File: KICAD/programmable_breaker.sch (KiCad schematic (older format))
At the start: 43 parts, among them Q1 BC847, Q2 BC847, Q3 BC847, U2 LM2903

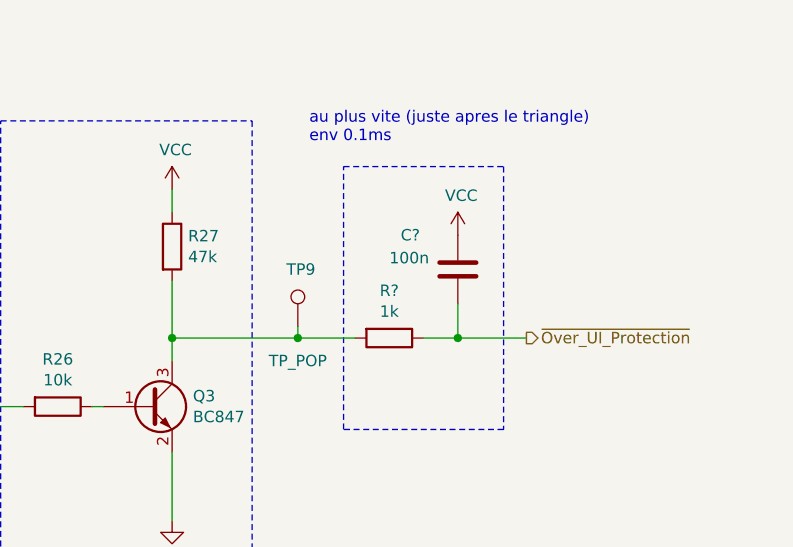
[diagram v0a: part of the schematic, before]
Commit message: edit footprints by jmt
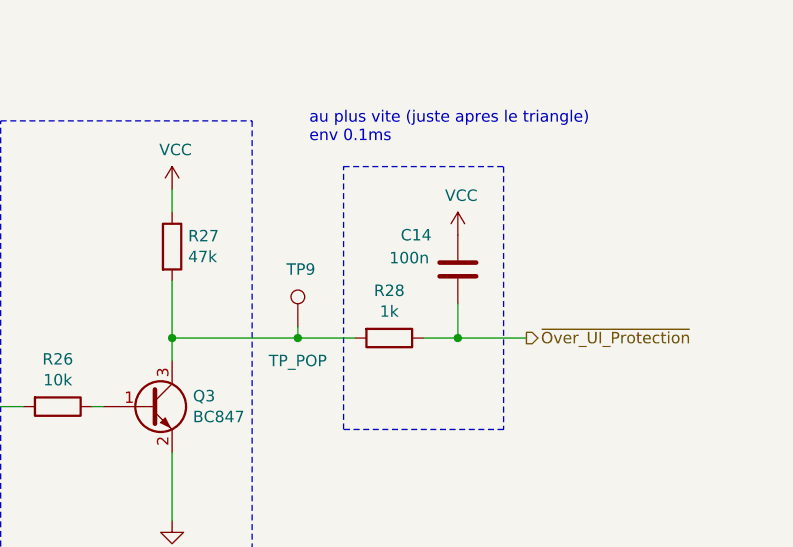
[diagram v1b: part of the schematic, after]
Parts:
- C10, C11, C6, C7, C8, C9: footprint (none) -> Capacitor_SMD:C_0805_2012Metric_Pad1.15x1.40mm_HandSolder
- C14: renamed from C?; footprint (none) -> Capacitor_SMD:C_0805_2012Metric_Pad1.15x1.40mm_HandSolder
- JP4, JP5, JP6, JP7, JP8, JP9: footprint (none) -> Connector_PinHeader_2.54mm:PinHeader_1x02_P2.54mm_Vertical
- R10, R11, R12, R13, R14, R15, R16, R17, R18, R19, R20, R21, R22, R23, R24, R25, R26, R27: footprint (none) -> Resistor_SMD:R_0805_2012Metric_Pad1.15x1.40mm_HandSolder
- R28: renamed from R?; footprint (none) -> Resistor_SMD:R_0805_2012Metric_Pad1.15x1.40mm_HandSolder
- TP5, TP6, TP8: footprint (none) -> TestPoint:TestPoint_THTPad_D2.0mm_Drill1.0mm
- TP7, TP9: footprint (none) -> TestPoint:TestPoint_Loop_D1.80mm_Drill1.0mm_Beaded
- U2: footprint (none) -> Package_SO:SO-8_5.3x6.2mm_P1.27mm

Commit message: route + work on djd
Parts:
- removed R28: 1k, Resistor_SMD:R_0805_2012Metric_Pad1.15x1.40mm_HandSolder, symbol Device:R
- C14: value 100n -> 470n
- R27: value 47k -> 10k
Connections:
- net GND: now also R27.2; no longer Q3.2 (E)
- net Rearm: now also Q1.1 (B), R24.1; no longer Q2.1 (B), R23.2
- net VCC: now also Q3.3 (C); no longer R27.1
- net ~Over_UI_Protection: now also Q3.2 (E), R27.1, TP9.1
- net at Q1.3 (C), R22.2, R23.1: no longer C11.1
- net S: now reaches TP7.1, U2.1, U2.7
- net S: now also Q2.1 (B), R23.2; no longer Q1.1 (B), R24.1
- net at Q2.3 (C), R24.2, R25.2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: now also C11.1
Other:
- note added: "4.7ms"
- note added: "47ms"
- note added: "A VOIR"
- note added: "Signal amp. & soft start"
- note removed: "Signal amp. & Invert"
- note removed: "au plus vite (juste apres le triangle)\nenv 0.1ms"
- moved on the sheet: C11, C14, Q1, Q2, Q3, R22, R23, R24, R25, R26, TP8, TP9

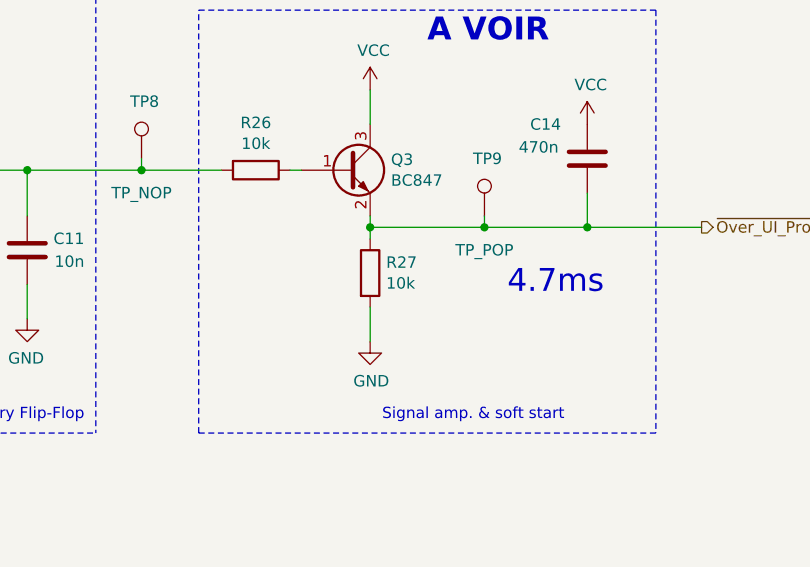
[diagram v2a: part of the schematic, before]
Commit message: added footprint for sepic coil + no more errors in netlist
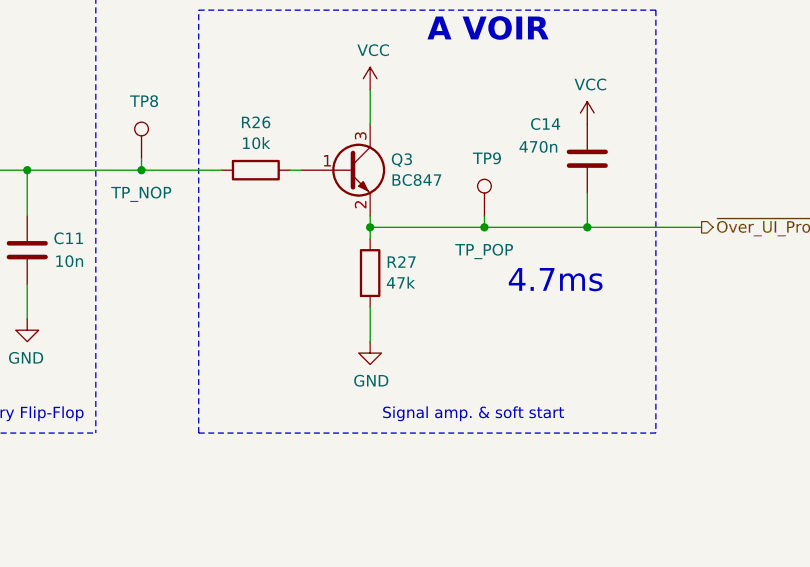
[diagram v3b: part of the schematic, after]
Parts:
- C10, C11, C14, C6, C7, C8, C9: footprint Capacitor_SMD:C_0805_2012Metric_Pad1.15x1.40mm_HandSolder -> Sesame_footprint:C_0805_2012Metric_Pad1.18x1.45mm_HandSolder
- R10, R11, R12, R13, R14, R15, R16, R17, R18, R19, R20, R21, R22, R23, R24, R25, R26: footprint Resistor_SMD:R_0805_2012Metric_Pad1.15x1.40mm_HandSolder -> Sesame_footprint:R_0805_2012Metric_Pad1.20x1.40mm_HandSolder
- R27: value 10k -> 47k; footprint Resistor_SMD:R_0805_2012Metric_Pad1.15x1.40mm_HandSolder -> Sesame_footprint:R_0805_2012Metric_Pad1.20x1.40mm_HandSolder
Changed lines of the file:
@@
 F 0 "R23" V 5957 2250 50  0000 C CNN
 F 1 "47k" V 5866 2250 50  0000 C CNN
-F 2 "Resistor_SMD:R_0805_2012Metric_Pad1.15x1.40mm_HandSolder" V 5680 2250 50  0001 C CNN
+F 2 "Sesame_footprint:R_0805_2012Metric_Pad1.20x1.40mm_HandSolder" V 5680 2250 50  0001 C CNN
 F 3 "~" H 5750 2250 50  0001 C CNN
 	1    5750 2250
@@
 F 0 "R24" V 6807 2250 50  0000 C CNN
 F 1 "47k" V 6716 2250 50  0000 C CNN
-F 2 "Resistor_SMD:R_0805_2012Metric_Pad1.15x1.40mm_HandSolder" V 6530 2250 50  0001 C CNN
+F 2 "Sesame_footprint:R_0805_2012Metric_Pad1.20x1.40mm_HandSolder" V 6530 2250 50  0001 C CNN
 F 3 "~" H 6600 2250 50  0001 C CNN
 	1    6600 2250
@@
 F 0 "R25" H 6970 1596 50  0000 L CNN
 F 1 "47k" H 6970 1505 50  0000 L CNN
-F 2 "Resistor_SMD:R_0805_2012Metric_Pad1.15x1.40mm_HandSolder" V 6830 1550 50  0001 C CNN
+F 2 "Sesame_footprint:R_0805_2012Metric_Pad1.20x1.40mm_HandSolder" V 6830 1550 50  0001 C CNN
 F 3 "~" H 6900 1550 50  0001 C CNN
 	1    6900 1550
@@
 F 0 "R22" H 5520 1596 50  0000 L CNN
 F 1 "47k" H 5520 1505 50  0000 L CNN
-F 2 "Resistor_SMD:R_0805_2012Metric_Pad1.15x1.40mm_HandSolder" V 5380 1550 50  0001 C CNN
+F 2 "Sesame_footprint:R_0805_2012Metric_Pad1.20x1.40mm_HandSolder" V 5380 1550 50  0001 C CNN
 F 3 "~" H 5450 1550 50  0001 C CNN
 	1    5450 1550
@@
 F 0 "C6" H 2765 6996 50  0000 L CNN
 F 1 "100n" H 2765 6905 50  0000 L CNN
-F 2 "Capacitor_SMD:C_0805_2012Metric_Pad1.15x1.40mm_HandSolder" H 2688 6800 50  0001 C CNN
+F 2 "Sesame_footprint:C_0805_2012Metric_Pad1.18x1.45mm_HandSolder" H 2688 6800 50  0001 C CNN
 F 3 "~" H 2650 6950 50  0001 C CNN
 	1    2650 6950
@@
 F 0 "R26" V 8143 2250 50  0000 C CNN
 F 1 "10k" V 8234 2250 50  0000 C CNN
-F 2 "Resistor_SMD:R_0805_2012Metric_Pad1.15x1.40mm_HandSolder" V 8280 2250 50  0001 C CNN
+F 2 "Sesame_footprint:R_0805_2012Metric_Pad1.20x1.40mm_HandSolder" V 8280 2250 50  0001 C CNN
 F 3 "~" H 8350 2250 50  0001 C CNN
 	1    8350 2250
@@
 F 0 "R20" V 3150 1850 50  0000 C CNN
 F 1 "100k" V 3050 1850 50  0000 C CNN
-F 2 "Resistor_SMD:R_0805_2012Metric_Pad1.15x1.40mm_HandSolder" V 2880 1850 50  0001 C CNN
+F 2 "Sesame_footprint:R_0805_2012Metric_Pad1.20x1.40mm_HandSolder" V 2880 1850 50  0001 C CNN
 F 3 "~" H 2950 1850 50  0001 C CNN
 	1    2950 1850
@@
 F 0 "C8" H 3515 2146 50  0000 L CNN
 F 1 "10n" H 3515 2055 50  0000 L CNN
-F 2 "Capacitor_SMD:C_0805_2012Metric_Pad1.15x1.40mm_HandSolder" H 3438 1950 50  0001 C CNN
+F 2 "Sesame_footprint:C_0805_2012Metric_Pad1.18x1.45mm_HandSolder" H 3438 1950 50  0001 C CNN
 F 3 "~" H 3400 2100 50  0001 C CNN
 	1    3400 2100
@@
 F 0 "R10" H 1020 2396 50  0000 L CNN
 F 1 "R" H 1020 2305 50  0000 L CNN
-F 2 "Resistor_SMD:R_0805_2012Metric_Pad1.15x1.40mm_HandSolder" V 880 2350 50  0001 C CNN
+F 2 "Sesame_footprint:R_0805_2012Metric_Pad1.20x1.40mm_HandSolder" V 880 2350 50  0001 C CNN
 F 3 "~" H 950 2350 50  0001 C CNN
 	1    950  2350
@@
 F 0 "R11" H 1020 2796 50  0000 L CNN
 F 1 "R" H 1020 2705 50  0000 L CNN
-F 2 "Resistor_SMD:R_0805_2012Metric_Pad1.15x1.40mm_HandSolder" V 880 2750 50  0001 C CNN
+F 2 "Sesame_footprint:R_0805_2012Metric_Pad1.20x1.40mm_HandSolder" V 880 2750 50  0001 C CNN
 F 3 "~" H 950 2750 50  0001 C CNN
 	1    950  2750
@@
 F 0 "R16" V 2300 1800 50  0000 C CNN
 F 1 "100k" V 2300 1600 50  0000 C CNN
-F 2 "Resistor_SMD:R_0805_2012Metric_Pad1.15x1.40mm_HandSolder" V 2330 1650 50  0001 C CNN
+F 2 "Sesame_footprint:R_0805_2012Metric_Pad1.20x1.40mm_HandSolder" V 2330 1650 50  0001 C CNN
 F 3 "~" H 2400 1650 50  0001 C CNN
 	1    2400 1650
@@
 F 0 "C7" H 3515 946 50  0000 L CNN
 F 1 "470n" H 3515 855 50  0000 L CNN
-F 2 "Capacitor_SMD:C_0805_2012Metric_Pad1.15x1.40mm_HandSolder" H 3438 750 50  0001 C CNN
+F 2 "Sesame_footprint:C_0805_2012Metric_Pad1.18x1.45mm_HandSolder" H 3438 750 50  0001 C CNN
 F 3 "~" H 3400 900 50  0001 C CNN
 	1    3400 900
@@
 F 0 "R14" V 2300 1300 50  0000 C CNN
 F 1 "100k" V 2300 1100 50  0000 C CNN
-F 2 "Resistor_SMD:R_0805_2012Metric_Pad1.15x1.40mm_HandSolder" V 2330 1150 50  0001 C CNN
+F 2 "Sesame_footprint:R_0805_2012Metric_Pad1.20x1.40mm_HandSolder" V 2330 1150 50  0001 C CNN
 F 3 "~" H 2400 1150 50  0001 C CNN
 	1    2400 1150
@@
 F 0 "R15" V 2300 1550 50  0000 C CNN
 F 1 "100k" V 2300 1350 50  0000 C CNN
-F 2 "Resistor_SMD:R_0805_2012Metric_Pad1.15x1.40mm_HandSolder" V 2330 1400 50  0001 C CNN
+F 2 "Sesame_footprint:R_0805_2012Metric_Pad1.20x1.40mm_HandSolder" V 2330 1400 50  0001 C CNN
 F 3 "~" H 2400 1400 50  0001 C CNN
 	1    2400 1400
@@
 F 0 "R21" V 3150 4650 50  0000 C CNN
 F 1 "100k" V 3050 4650 50  0000 C CNN
-F 2 "Resistor_SMD:R_0805_2012Metric_Pad1.15x1.40mm_HandSolder" V 2880 4650 50  0001 C CNN
+F 2 "Sesame_footprint:R_0805_2012Metric_Pad1.20x1.40mm_HandSolder" V 2880 4650 50  0001 C CNN
 F 3 "~" H 2950 4650 50  0001 C CNN
 	1    2950 4650
@@
 F 0 "C10" H 3515 4946 50  0000 L CNN
 F 1 "10n" H 3515 4855 50  0000 L CNN
-F 2 "Capacitor_SMD:C_0805_2012Metric_Pad1.15x1.40mm_HandSolder" H 3438 4750 50  0001 C CNN
+F 2 "Sesame_footprint:C_0805_2012Metric_Pad1.18x1.45mm_HandSolder" H 3438 4750 50  0001 C CNN
 F 3 "~" H 3400 4900 50  0001 C CNN
 	1    3400 4900
@@
 F 0 "R12" H 1020 5196 50  0000 L CNN
 F 1 "R" H 1020 5105 50  0000 L CNN
-F 2 "Resistor_SMD:R_0805_2012Metric_Pad1.15x1.40mm_HandSolder" V 880 5150 50  0001 C CNN
+F 2 "Sesame_footprint:R_0805_2012Metric_Pad1.20x1.40mm_HandSolder" V 880 5150 50  0001 C CNN
 F 3 "~" H 950 5150 50  0001 C CNN
 	1    950  5150
@@
 F 0 "R13" H 1020 5596 50  0000 L CNN
 F 1 "R" H 1020 5505 50  0000 L CNN
-F 2 "Resistor_SMD:R_0805_2012Metric_Pad1.15x1.40mm_HandSolder" V 880 5550 50  0001 C CNN
+F 2 "Sesame_footprint:R_0805_2012Metric_Pad1.20x1.40mm_HandSolder" V 880 5550 50  0001 C CNN
 F 3 "~" H 950 5550 50  0001 C CNN
 	1    950  5550
@@
 F 0 "R19" V 2300 4600 50  0000 C CNN
 F 1 "100k" V 2300 4400 50  0000 C CNN
-F 2 "Resistor_SMD:R_0805_2012Metric_Pad1.15x1.40mm_HandSolder" V 2330 4450 50  0001 C CNN
+F 2 "Sesame_footprint:R_0805_2012Metric_Pad1.20x1.40mm_HandSolder" V 2330 4450 50  0001 C CNN
 F 3 "~" H 2400 4450 50  0001 C CNN
 	1    2400 4450
@@
 F 0 "C9" H 3515 3746 50  0000 L CNN
 F 1 "470n" H 3515 3655 50  0000 L CNN
-F 2 "Capacitor_SMD:C_0805_2012Metric_Pad1.15x1.40mm_HandSolder" H 3438 3550 50  0001 C CNN
+F 2 "Sesame_footprint:C_0805_2012Metric_Pad1.18x1.45mm_HandSolder" H 3438 3550 50  0001 C CNN
 F 3 "~" H 3400 3700 50  0001 C CNN
 	1    3400 3700
@@
 F 0 "R17" V 2300 4100 50  0000 C CNN
 F 1 "100k" V 2300 3900 50  0000 C CNN
-F 2 "Resistor_SMD:R_0805_2012Metric_Pad1.15x1.40mm_HandSolder" V 2330 3950 50  0001 C CNN
+F 2 "Sesame_footprint:R_0805_2012Metric_Pad1.20x1.40mm_HandSolder" V 2330 3950 50  0001 C CNN
 F 3 "~" H 2400 3950 50  0001 C CNN
 	1    2400 3950
@@
 F 0 "R18" V 2300 4350 50  0000 C CNN
 F 1 "100k" V 2300 4150 50  0000 C CNN
-F 2 "Resistor_SMD:R_0805_2012Metric_Pad1.15x1.40mm_HandSolder" V 2330 4200 50  0001 C CNN
+F 2 "Sesame_footprint:R_0805_2012Metric_Pad1.20x1.40mm_HandSolder" V 2330 4200 50  0001 C CNN
 F 3 "~" H 2400 4200 50  0001 C CNN
 	1    2400 4200
@@
 F 0 "C14" H 9550 2350 50  0000 L CNN
 F 1 "470n" H 9500 2250 50  0000 L CNN
-F 2 "Capacitor_SMD:C_0805_2012Metric_Pad1.15x1.40mm_HandSolder" H 9838 2050 50  0001 C CNN
+F 2 "Sesame_footprint:C_0805_2012Metric_Pad1.18x1.45mm_HandSolder" H 9838 2050 50  0001 C CNN
 F 3 "~" H 9800 2200 50  0001 C CNN
 	1    9800 2200
@@
 	4550 1750 4850 1750
 Connection ~ 4850 1750
-$Comp
-L Device:R R27
-U 1 1 61298257
-P 8850 2700
-F 0 "R27" H 8920 2746 50  0000 L CNN
-F 1 "10k" H 8920 2655 50  0000 L CNN
-F 2 "Resistor_SMD:R_0805_2012Metric_Pad1.15x1.40mm_HandSolder" V 8780 2700 50  0001 C CNN
-F 3 "~" H 8850 2700 50  0001 C CNN
-	1    8850 2700
-	1    0    0    -1
-$EndComp
 Wire Wire Line
 	8850 2550 8850 2500
@@
 F 0 "C11" H 7100 2650 50  0000 L CNN
 F 1 "10n" H 7100 2550 50  0000 L CNN
-F 2 "Capacitor_SMD:C_0805_2012Metric_Pad1.15x1.40mm_HandSolder" H 7388 2450 50  0001 C CNN
+F 2 "Sesame_footprint:C_0805_2012Metric_Pad1.18x1.45mm_HandSolder" H 7388 2450 50  0001 C CNN
 F 3 "~" H 7350 2600 50  0001 C CNN
 	1    7350 2600
@@
 Text Notes 9100 1700 0    100  ~ 20
 A VOIR
+$Comp
+L Device:R R27
+U 1 1 6127338C
+P 8850 2700
+F 0 "R27" H 8920 2746 50  0000 L CNN
+F 1 "47k" H 8920 2655 50  0000 L CNN
+F 2 "Sesame_footprint:R_0805_2012Metric_Pad1.20x1.40mm_HandSolder" V 8780 2700 50  0001 C CNN
+F 3 "~" H 8850 2700 50  0001 C CNN
+	1    8850 2700
+	1    0    0    -1
+$EndComp
 $EndSCHEMATC

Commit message: lil cleanup on the main schematic sheet
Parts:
- C10, C11, C14, C6, C7, C8, C9: symbol Device:C -> sesame-fonctionnel-rescue:C-Device
- JP4, JP5, JP6, JP7, JP8, JP9: symbol Device:Jumper -> sesame-fonctionnel-rescue:Jumper-Device
- Q1, Q2, Q3: symbol Transistor_BJT:BC847 -> sesame-fonctionnel-rescue:BC847-Transistor_BJT
- R10, R11, R12, R13, R14, R15, R16, R17, R18, R19, R20, R21, R22, R23, R24, R25, R26, R27: symbol Device:R -> sesame-fonctionnel-rescue:R-Device
- RV2, RV3: symbol Device:R_POT -> sesame-fonctionnel-rescue:R_POT-Device
- TP5, TP6, TP7, TP8, TP9: symbol Connector:TestPoint -> sesame-fonctionnel-rescue:TestPoint-Connector
- U2: symbol Comparator:LM2903 -> sesame-fonctionnel-rescue:LM2903-Comparator
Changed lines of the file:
@@
 Voltage_Sens
 $Comp
-L Device:R R23
+L sesame-fonctionnel-rescue:R-Device R23
 U 1 1 610C1787
 P 5750 2250
@@
 $EndComp
 $Comp
-L Device:R R24
+L sesame-fonctionnel-rescue:R-Device R24
 U 1 1 610C1C9F
 P 6600 2250
@@
 $EndComp
 $Comp
-L Device:R R25
+L sesame-fonctionnel-rescue:R-Device R25
 U 1 1 610C1F6B
 P 6900 1550
@@
 $EndComp
 $Comp
-L Device:R R22
+L sesame-fonctionnel-rescue:R-Device R22
 U 1 1 610C2293
 P 5450 1550
@@
 $EndComp
 $Comp
-L Transistor_BJT:BC847 Q2
+L sesame-fonctionnel-rescue:BC847-Transistor_BJT Q2
 U 1 1 610C3843
 P 6800 2600
@@
 $EndComp
 $Comp
-L Transistor_BJT:BC847 Q1
+L sesame-fonctionnel-rescue:BC847-Transistor_BJT Q1
 U 1 1 610C6206
 P 5550 2600
@@
 Connection ~ 6900 2250
 $Comp
-L Transistor_BJT:BC847 Q3
+L sesame-fonctionnel-rescue:BC847-Transistor_BJT Q3
 U 1 1 610CECBF
 P 8750 2250
@@
 $EndComp
 $Comp
-L power:GND #PWR029
+L sesame-fonctionnel-rescue:GND-power #PWR029
 U 1 1 610D4337
 P 6900 2950
@@
 $EndComp
 $Comp
-L power:GND #PWR027
+L sesame-fonctionnel-rescue:GND-power #PWR027
 U 1 1 610D4AD2
 P 5450 2950
@@
 	6900 2800 6900 2950
 $Comp
-L Device:C C6
+L sesame-fonctionnel-rescue:C-Device C6
 U 1 1 611101E3
 P 2650 6950
@@
 	2650 7300 2650 7100
 $Comp
-L power:GND #PWR020
+L sesame-fonctionnel-rescue:GND-power #PWR020
 U 1 1 61146881
 P 2450 7400
@@
 Alim. AOP
 $Comp
-L Device:R R26
+L sesame-fonctionnel-rescue:R-Device R26
 U 1 1 6131658A
 P 8350 2250
@@
 	5050 950  5050 3400
 $Comp
-L Device:R R20
+L sesame-fonctionnel-rescue:R-Device R20
 U 1 1 611CE01D
 P 2950 1850
@@
 	3950 1850 3400 1850
 $Comp
-L Device:C C8
+L sesame-fonctionnel-rescue:C-Device C8
 U 1 1 611CE03F
 P 3400 2100
@@
 $EndComp
 $Comp
-L power:GND #PWR022
+L sesame-fonctionnel-rescue:GND-power #PWR022
 U 1 1 611CE048
 P 3400 2250
@@
 $EndComp
 $Comp
-L Device:Jumper JP4
+L sesame-fonctionnel-rescue:Jumper-Device JP4
 U 1 1 611CE04F
 P 3100 1150
@@
 $EndComp
 $Comp
-L Device:Jumper JP5
+L sesame-fonctionnel-rescue:Jumper-Device JP5
 U 1 1 611CE055
 P 3100 1400
@@
 $EndComp
 $Comp
-L Device:Jumper JP6
+L sesame-fonctionnel-rescue:Jumper-Device JP6
 U 1 1 611CE05B
 P 3100 1650
@@
 Voltage_Thres
 $Comp
-L power:GND #PWR014
+L sesame-fonctionnel-rescue:GND-power #PWR014
 U 1 1 611DFB26
 P 950 2900
@@
 $EndComp
 $Comp
-L Device:R_POT RV2
+L sesame-fonctionnel-rescue:R_POT-Device RV2
 U 1 1 611DFB2C
 P 950 1150
@@
 $EndComp
 $Comp
-L power:GND #PWR012
+L sesame-fonctionnel-rescue:GND-power #PWR012
 U 1 1 611DFB32
 P 950 1300
@@
 $EndComp
 $Comp
-L Device:R R10
+L sesame-fonctionnel-rescue:R-Device R10
 U 1 1 611DFB44
 P 950 2350
@@
 $EndComp
 $Comp
-L Device:R R11
+L sesame-fonctionnel-rescue:R-Device R11
 U 1 1 611DFB4A
 P 950 2750
@@
 	2450 6600 2650 6600
 $Comp
-L Device:R R16
+L sesame-fonctionnel-rescue:R-Device R16
 U 1 1 611E6403
 P 2400 1650
@@
 S
 $Comp
-L Device:C C7
+L sesame-fonctionnel-rescue:C-Device C7
 U 1 1 6139E3D0
 P 3400 900
@@
 Connection ~ 3400 1150
 $Comp
-L Device:R R14
+L sesame-fonctionnel-rescue:R-Device R14
 U 1 1 613A87CC
 P 2400 1150
@@
 	2550 1650 2800 1650
 $Comp
-L Device:R R15
+L sesame-fonctionnel-rescue:R-Device R15
 U 1 1 613C276D
 P 2400 1400
@@
 $EndComp
 $Comp
-L power:VCC #PWR026
+L sesame-fonctionnel-rescue:VCC-power #PWR026
 U 1 1 614D7D88
 P 5450 1300
@@
 $EndComp
 $Comp
-L power:VCC #PWR028
+L sesame-fonctionnel-rescue:VCC-power #PWR028
 U 1 1 614D95EF
 P 6900 1300
@@
 	6900 1300 6900 1400
 $Comp
-L power:VCC #PWR019
+L sesame-fonctionnel-rescue:VCC-power #PWR019
 U 1 1 614E8D13
 P 2450 6550
@@
 Current comparator\n(Over current)
 $Comp
-L Device:R R21
+L sesame-fonctionnel-rescue:R-Device R21
 U 1 1 615178DC
 P 2950 4650
@@
 $EndComp
 $Comp
-L Device:C C10
+L sesame-fonctionnel-rescue:C-Device C10
 U 1 1 615178FE
 P 3400 4900
@@
 $EndComp
 $Comp
-L power:GND #PWR024
+L sesame-fonctionnel-rescue:GND-power #PWR024
 U 1 1 61517905
 P 3400 5050
@@
 $EndComp
 $Comp
-L Device:Jumper JP7
+L sesame-fonctionnel-rescue:Jumper-Device JP7
 U 1 1 6151790B
 P 3100 3950
@@
 $EndComp
 $Comp
-L Device:Jumper JP8
+L sesame-fonctionnel-rescue:Jumper-Device JP8
 U 1 1 61517911
 P 3100 4200
@@
 $EndComp
 $Comp
-L Device:Jumper JP9
+L sesame-fonctionnel-rescue:Jumper-Device JP9
 U 1 1 61517917
 P 3100 4450
@@
 	3400 4200 3400 4450
 $Comp
-L power:GND #PWR018
+L sesame-fonctionnel-rescue:GND-power #PWR018
 U 1 1 61517925
 P 950 5700
@@
 $EndComp
 $Comp
-L Device:R_POT RV3
+L sesame-fonctionnel-rescue:R_POT-Device RV3
 U 1 1 6151792B
 P 950 3950
@@
 $EndComp
 $Comp
-L power:GND #PWR016
+L sesame-fonctionnel-rescue:GND-power #PWR016
 U 1 1 61517931
 P 950 4100
@@
 $EndComp
 $Comp
-L Device:R R12
+L sesame-fonctionnel-rescue:R-Device R12
 U 1 1 61517937
 P 950 5150
@@
 $EndComp
 $Comp
-L Device:R R13
+L sesame-fonctionnel-rescue:R-Device R13
 U 1 1 6151793D
 P 950 5550
@@
 	950  5350 950  5300
 $Comp
-L Device:R R19
+L sesame-fonctionnel-rescue:R-Device R19
 U 1 1 61517948
 P 2400 4450
@@
 	2150 3300 2150 5300
 $Comp
-L Device:C C9
+L sesame-fonctionnel-rescue:C-Device C9
 U 1 1 61517958
 P 3400 3700
@@
 Connection ~ 3400 3950
 $Comp
-L Device:R R17
+L sesame-fonctionnel-rescue:R-Device R17
 U 1 1 61517960
 P 2400 3950
@@
 	2550 4450 2800 4450
 $Comp
-L Device:R R18
+L sesame-fonctionnel-rescue:R-Device R18
 U 1 1 6151796A
 P 2400 4200
@@
 	1350 4700 1350 6200
 $Comp
-L Comparator:LM2903 U2
+L sesame-fonctionnel-rescue:LM2903-Comparator U2
 U 1 1 611D87A4
 P 4250 1750
@@
 $EndComp
 $Comp
-L Comparator:LM2903 U2
+L sesame-fonctionnel-rescue:LM2903-Comparator U2
 U 2 1 611EA33A
 P 4250 4550
@@
 $EndComp
 $Comp
-L Comparator:LM2903 U2
+L sesame-fonctionnel-rescue:LM2903-Comparator U2
 U 3 1 6120EB61
 P 2350 6950
@@
 $EndComp
 $Comp
-L Connector:TestPoint TP5
+L sesame-fonctionnel-rescue:TestPoint-Connector TP5
 U 1 1 6130058F
 P 3750 1600
@@
 	3750 1650 3950 1650
 $Comp
-L Connector:TestPoint TP6
+L sesame-fonctionnel-rescue:TestPoint-Connector TP6
 U 1 1 613059B5
 P 3750 4400
@@
 	3750 4450 3950 4450
 $Comp
-L Connector:TestPoint TP9
+L sesame-fonctionnel-rescue:TestPoint-Connector TP9
 U 1 1 6130815B
 P 9350 2450
@@
 	3950 4650 3400 4650
 $Comp
-L Connector:TestPoint TP8
+L sesame-fonctionnel-rescue:TestPoint-Connector TP8
 U 1 1 6157044B
 P 7850 2200
@@
 	7850 2250 8200 2250
 $Comp
-L Connector:TestPoint TP7
+L sesame-fonctionnel-rescue:TestPoint-Connector TP7
 U 1 1 61584A92
 P 4850 1700
@@
 	5650 3600 6000 3600
 $Comp
-L power:GND #PWR031
+L sesame-fonctionnel-rescue:GND-power #PWR031
 U 1 1 610D4EC6
 P 8850 3000
@@
 	9800 2500 10300 2500
 $Comp
-L power:VCC #PWR039
+L sesame-fonctionnel-rescue:VCC-power #PWR039
 U 1 1 61BFDB95
 P 9800 2050
@@
 Connection ~ 9800 2500
 $Comp
-L Device:C C14
+L sesame-fonctionnel-rescue:C-Device C14
 U 1 1 61BFDBA3
 P 9800 2200
@@
 4.7ms
 $Comp
-L Device:C C11
+L sesame-fonctionnel-rescue:C-Device C11
 U 1 1 610FF241
 P 7350 2600
@@
 $EndComp
 $Comp
-L power:GND #PWR025
+L sesame-fonctionnel-rescue:GND-power #PWR025
 U 1 1 6110DB40
 P 7350 2900
@@
 	8850 2500 8850 2450
 $Comp
-L power:VCC #PWR0133
+L sesame-fonctionnel-rescue:VCC-power #PWR0133
 U 1 1 6132B6E2
 P 8850 1900
@@
 A VOIR
 $Comp
-L Device:R R27
+L sesame-fonctionnel-rescue:R-Device R27
 U 1 1 6127338C
 P 8850 2700
